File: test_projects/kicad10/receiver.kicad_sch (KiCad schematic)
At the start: 43 parts, among them U1 ASDMB-xxxMHz, U2 ADV7611

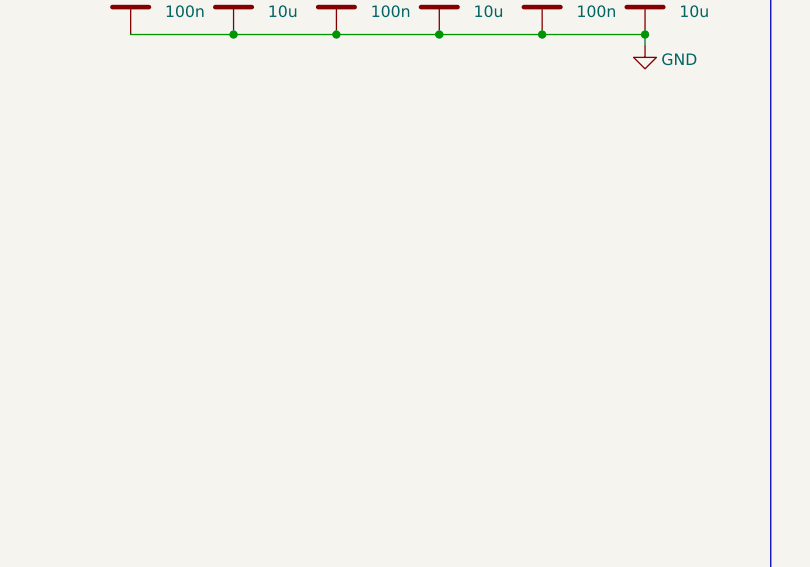
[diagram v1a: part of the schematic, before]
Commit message: [#89355] test_projects: K10: Add additional features
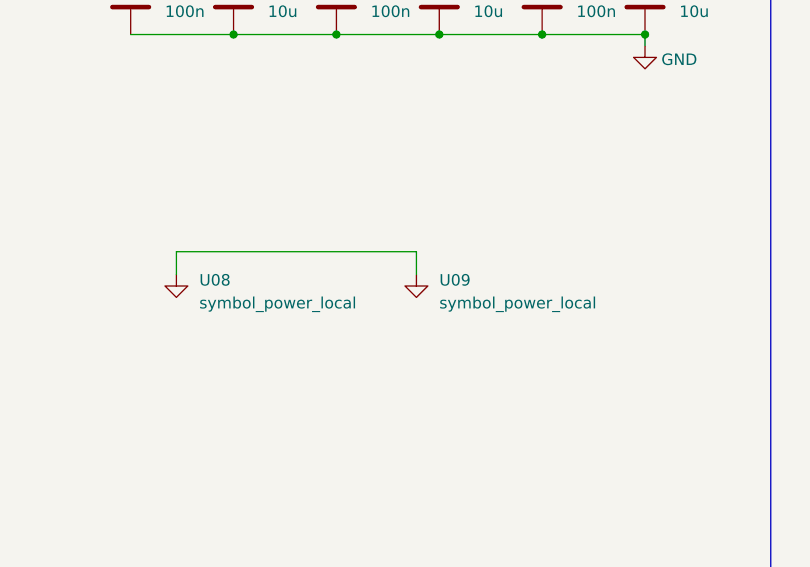
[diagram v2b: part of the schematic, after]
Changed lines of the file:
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@@
 (kicad_sch
-	(version 20260101)
+	(version 20260306)
 	(generator "eeschema")
 	(generator_version "10.0")
@@
 	(wire
 		(pts
+			(xy 58.42 161.29) (xy 58.42 163.83)
+		)
+		(stroke
+			(width 0)
+			(type default)
+		)
+	)
+	(wire
+		(pts
 			(xy 135.89 76.2) (xy 135.89 78.74)
 		)
@@
 	(wire
 		(pts
+			(xy 85.09 161.29) (xy 58.42 161.29)
+		)
+		(stroke
+			(width 0)
+			(type default)
+		)
+	)
+	(wire
+		(pts
 			(xy 76.2 72.39) (xy 87.63 72.39)
 		)
@@
 	(wire
 		(pts
+			(xy 85.09 163.83) (xy 85.09 161.29)
+		)
+		(stroke
+			(width 0)
+			(type default)
+		)
+	)
+	(wire
+		(pts
 			(xy 87.63 120.65) (xy 99.06 120.65)
 		)
@@
 		)
 		(instances
-			(project ""
+			(project "test_project"
 				(path "/59f522e0-0cf7-48a6-bc09-47b340553d24/0dda78d5-f05b-4dcc-877d-5ed0c0f73913"
 					(reference "R1")
@@
 		)
 		(instances
-			(project ""
+			(project "test_project"
 				(path "/59f522e0-0cf7-48a6-bc09-47b340553d24/0dda78d5-f05b-4dcc-877d-5ed0c0f73913"
 					(reference "C3")
@@
 		)
 		(instances
-			(project ""
+			(project "test_project"
 				(path "/59f522e0-0cf7-48a6-bc09-47b340553d24/0dda78d5-f05b-4dcc-877d-5ed0c0f73913"
 					(reference "R6")
@@
 		)
 		(instances
-			(project ""
+			(project "test_project"
 				(path "/59f522e0-0cf7-48a6-bc09-47b340553d24/0dda78d5-f05b-4dcc-877d-5ed0c0f73913"
 					(reference "C14")
@@
 	)
 	(symbol
+		(lib_id "askiff_test_symbols_split:symbol_power_local")
+		(at 58.42 165.1 0)
+		(unit 1)
+		(body_style 1)
+		(exclude_from_sim yes)
+		(in_bom no)
+		(on_board no)
+		(in_pos_files yes)
+		(dnp no)
+		(fields_autoplaced yes)
+		(property "Reference" "U08"
+			(at 60.96 164.4649 0)
+			(show_name no)
+			(do_not_autoplace no)
+			(effects
+				(font
+					(size 1.27 1.27)
+				)
+				(justify left)
+			)
+		)
+		(property "Value" "symbol_power_local"
+			(at 60.96 167.0049 0)
+			(show_name no)
+			(do_not_autoplace no)
+			(effects
+				(font
+					(size 1.27 1.27)
+				)
+				(justify left)
+			)
+		)
+		(property "Footprint" ""
+			(at 58.42 165.1 0)
+			(hide yes)
+			(show_name no)
+			(do_not_autoplace no)
+			(effects
+				(font
+					(size 1.27 1.27)
+				)
+			)
+		)
+		(property "Datasheet" ""
+			(at 58.42 165.1 0)
+			(hide yes)
+			(show_name no)
+			(do_not_autoplace no)
+			(effects
+				(font
+					(size 1.27 1.27)
+				)
+			)
+		)
+		(property "Description" ""
+			(at 58.42 165.1 0)
+			(hide yes)
+			(show_name no)
+			(do_not_autoplace no)
+			(effects
+				(font
+					(size 1.27 1.27)
+				)
+			)
+		)
+		(pin ""
+		)
+		(instances
+			(project "test_project"
+				(path "/59f522e0-0cf7-48a6-bc09-47b340553d24/0dda78d5-f05b-4dcc-877d-5ed0c0f73913"
+					(reference "U08")
+					(unit 1)
+				)
+			)
+		)
+	)
+	(symbol
 		(lib_id "Device:R")
 		(at 135.89 72.39 0)
@@
 		)
 		(instances
-			(project ""
+			(project "test_project"
 				(path "/59f522e0-0cf7-48a6-bc09-47b340553d24/0dda78d5-f05b-4dcc-877d-5ed0c0f73913"
 					(reference "#PWR043")
@@
 	)
 	(symbol
+		(lib_id "askiff_test_symbols_split:symbol_power_local")
+		(at 85.09 165.1 0)
+		(unit 1)
+		(body_style 1)
+		(exclude_from_sim yes)
+		(in_bom no)
+		(on_board no)
+		(in_pos_files yes)
+		(dnp no)
+		(fields_autoplaced yes)
+		(property "Reference" "U09"
+			(at 87.63 164.4649 0)
+			(show_name no)
+			(do_not_autoplace no)
+			(effects
+				(font
+					(size 1.27 1.27)
+				)
+				(justify left)
+			)
+		)
+		(property "Value" "symbol_power_local"
+			(at 87.63 167.0049 0)
+			(show_name no)
+			(do_not_autoplace no)
+			(effects
+				(font
+					(size 1.27 1.27)
+				)
+				(justify left)
+			)
+		)
+		(property "Footprint" ""
+			(at 85.09 165.1 0)
+			(hide yes)
+			(show_name no)
+			(do_not_autoplace no)
+			(effects
+				(font
+					(size 1.27 1.27)
+				)
+			)
+		)
+		(property "Datasheet" ""
+			(at 85.09 165.1 0)
+			(hide yes)
+			(show_name no)
+			(do_not_autoplace no)
+			(effects
+				(font
+					(size 1.27 1.27)
+				)
+			)
+		)
+		(property "Description" ""
+			(at 85.09 165.1 0)
+			(hide yes)
+			(show_name no)
+			(do_not_autoplace no)
+			(effects
+				(font
+					(size 1.27 1.27)
+				)
+			)
+		)
+		(pin ""
+		)
+		(instances
+			(project "test_project"
+				(path "/59f522e0-0cf7-48a6-bc09-47b340553d24/0dda78d5-f05b-4dcc-877d-5ed0c0f73913"
+					(reference "U09")
+					(unit 1)
+				)
+			)
+		)
+	)
+	(symbol
 		(lib_id "Device:C")
 		(at 110.49 76.2 0)
@@
 		)
 		(instances
-			(project ""
+			(project "test_project"
 				(path "/59f522e0-0cf7-48a6-bc09-47b340553d24/0dda78d5-f05b-4dcc-877d-5ed0c0f73913"
 					(reference "#PWR027")
@@
 		)
 		(instances
-			(project ""
+			(project "test_project"
 				(path "/59f522e0-0cf7-48a6-bc09-47b340553d24/0dda78d5-f05b-4dcc-877d-5ed0c0f73913"
 					(reference "#PWR07")
@@
 		)
 	)
+	(group "DVDDIO Decoupling"
+		(members "0226e162-ac91-452c-afa0-2ea4b0b44746" "0688ef5c-f4c4-4593-af41-7f375f01958e"
+			"26777a73-c41f-452f-a4ca-9708228bd6d4" "335f4949-ffe9-4938-9d57-cf815b3b0b29"
+			"53919c59-e35c-4792-83f0-395a1fd86dbd" "53a75b28-229b-402c-9b6b-0cec0055aa37"
+			"619f5ae0-a754-4d54-a168-8b79aa89670c" "6d133988-e558-476c-8572-5f02e2e5a6c6"
+			"743c8518-554b-42eb-87ad-496b211ebd7e" "7722cf08-dc1e-44b9-b817-6ce153d7d63a"
+			"7e3a62fa-3ba2-4b66-9cef-d3f8730bdeeb" "8a9b63c3-cc97-40e5-a4ae-a7054bc2e7e3"
+			"8ef9520e-611d-4a87-b33b-5255acc4c13b" "9655f55b-5911-4dd7-83ad-bb28b385dacf"
+			"9ced7b9d-c205-44c1-a7c4-c9a229d89ced" "a4d87169-0858-4a21-bfe5-4ae9c856a947"
+			"a67f5433-ffb1-4a64-a695-e3d941a5c473" "aa1e8489-6b05-4619-b55f-df85adba8db6"
+			"aaa87def-6a20-4fb9-9d5a-a4f952fd4cc4" "ad9c8ed4-d178-4747-9f9c-78d78d474be6"
+			"b4b21dc7-871a-4217-945b-af2420411a37" "b761d0df-8de4-468e-8aab-73364b2695bc"
+			"bba9207e-cbd3-4c81-8ae8-646803c1c004" "c0a00dc3-c2ae-41c6-bb0b-71d5629a13b7"
+			"d47eceae-cecb-441e-990d-61f23539cbac" "d646e2da-db48-49d3-8198-95eb99b83ede"
+			"ee9d4c75-60d8-4c04-a22e-9da0b8e55f17" "f1e8db82-cfcd-4010-a45e-35db3e4b33d3"
+			"f867189b-b072-4acc-b2b7-4722a94bd22f" "ff9f44fd-0c56-4787-a533-40ed924f1b42"
+		)
+	)
